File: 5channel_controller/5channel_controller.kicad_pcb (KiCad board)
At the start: 2 copper layers, 68.6 x 47.6 mm, 60 parts, among them J1 UART, J2 PWR, J3 LED1, J4 LED2, J5 LED3, J6 LED4, J7 LED5, SW1 SW_RST, SW2 SW_PROG, U1 CAT4101, U2 ESP-12E, U3 CAT4101, U4 LM1117-3.3, U5 CAT4101, U6 PCA9685PW, U7 CAT4101, U8 CAT4101

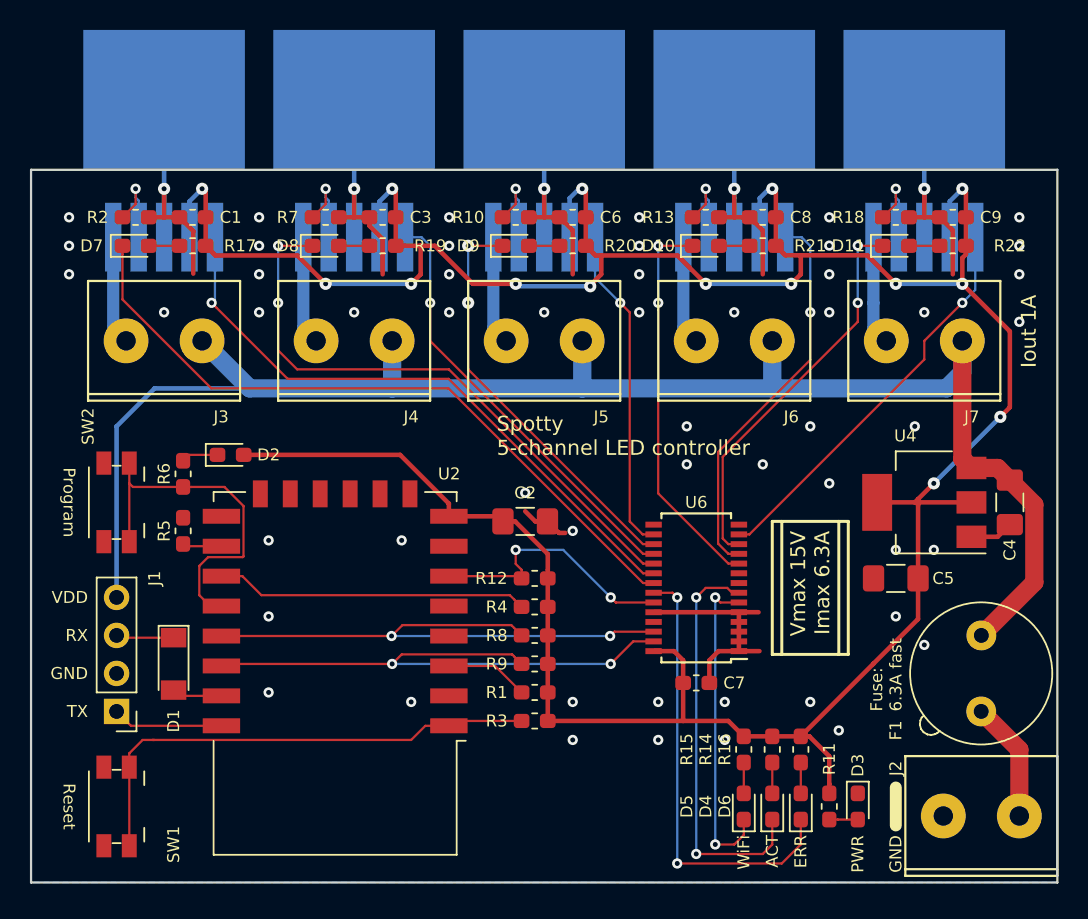
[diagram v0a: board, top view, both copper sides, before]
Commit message: Add header for external temperature sensor
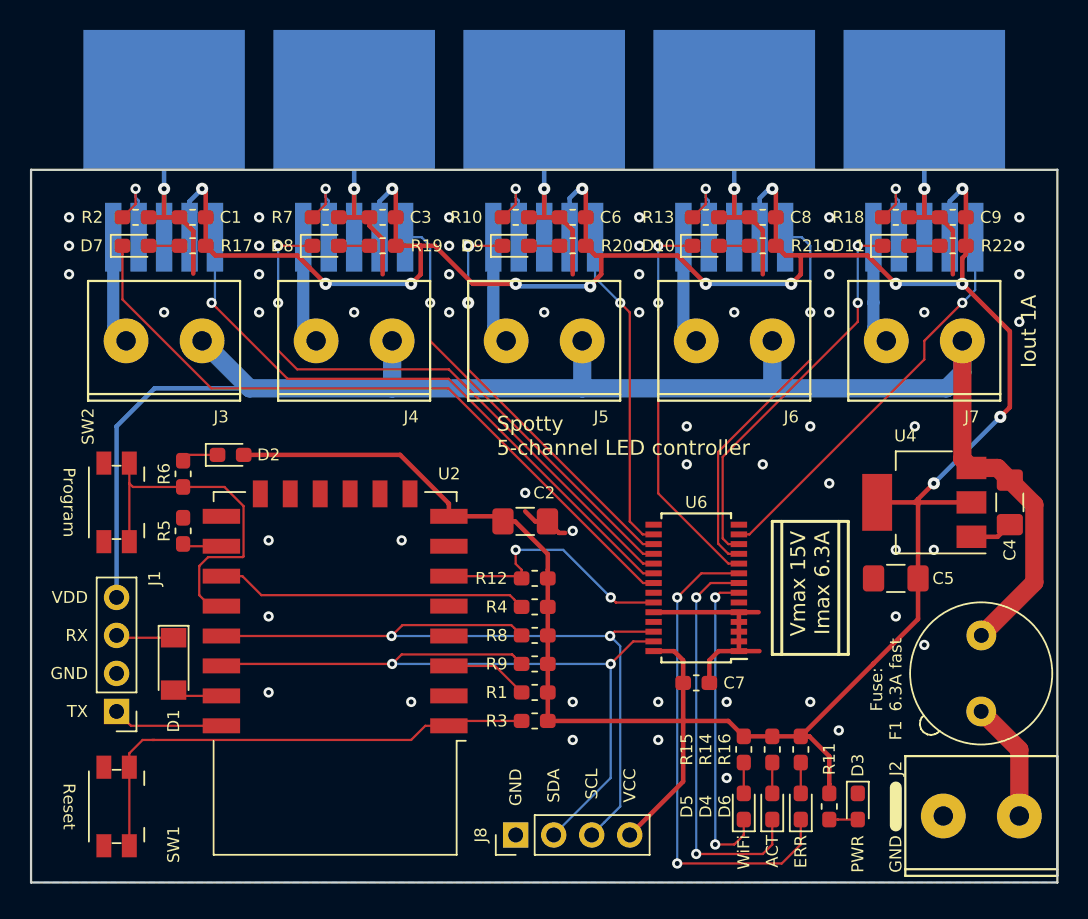
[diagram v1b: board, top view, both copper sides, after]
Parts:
- added J8: UART, Connector_PinHeader_2.54mm:PinHeader_1x04_P2.54mm_Vertical, F.Cu at (71.8, 91.4)
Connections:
- U2 pad 10: Net-(U2-Pad10) -> (no net)
- U2 pad 11: Net-(U2-Pad11) -> (no net)
- U2 pad 12: Net-(U2-Pad12) -> (no net)
- U2 pad 13: Net-(U2-Pad13) -> (no net)
- U2 pad 14: Net-(U2-Pad14) -> (no net)
- U2 pad 2: Net-(U2-Pad2) -> (no net)
- U2 pad 4: Net-(U2-Pad4) -> (no net)
- U2 pad 5: Net-(U2-Pad5) -> (no net)
- U2 pad 7: Net-(U2-Pad7) -> (no net)
- U2 pad 9: Net-(U2-Pad9) -> (no net)
- U6 pad 15: Net-(U6-Pad15) -> (no net)
- U6 pad 22: DispERR -> (no net)
- U6 pad 25: Net-(U6-Pad25) -> (no net)
- U6 pad 6: DispWiFi -> (no net)
- U6 pad 7: DispACT -> DispWiFi
- U6 pad 8: Net-(U6-Pad8) -> DispACT
- U6 pad 9: Net-(U6-Pad9) -> DispERR
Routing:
- net SCL: track 38.4 -> 52.7 mm
- net SDA: track 38.7 -> 51.7 mm
- net VCC: track 211.9 -> 221.0 mm
- net DispERR: track 29.9 -> 33.0 mm
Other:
- board text added: "SCL"
- board text added: "SDA"
- board text added: "VCC"
